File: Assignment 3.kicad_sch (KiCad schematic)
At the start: 1 part

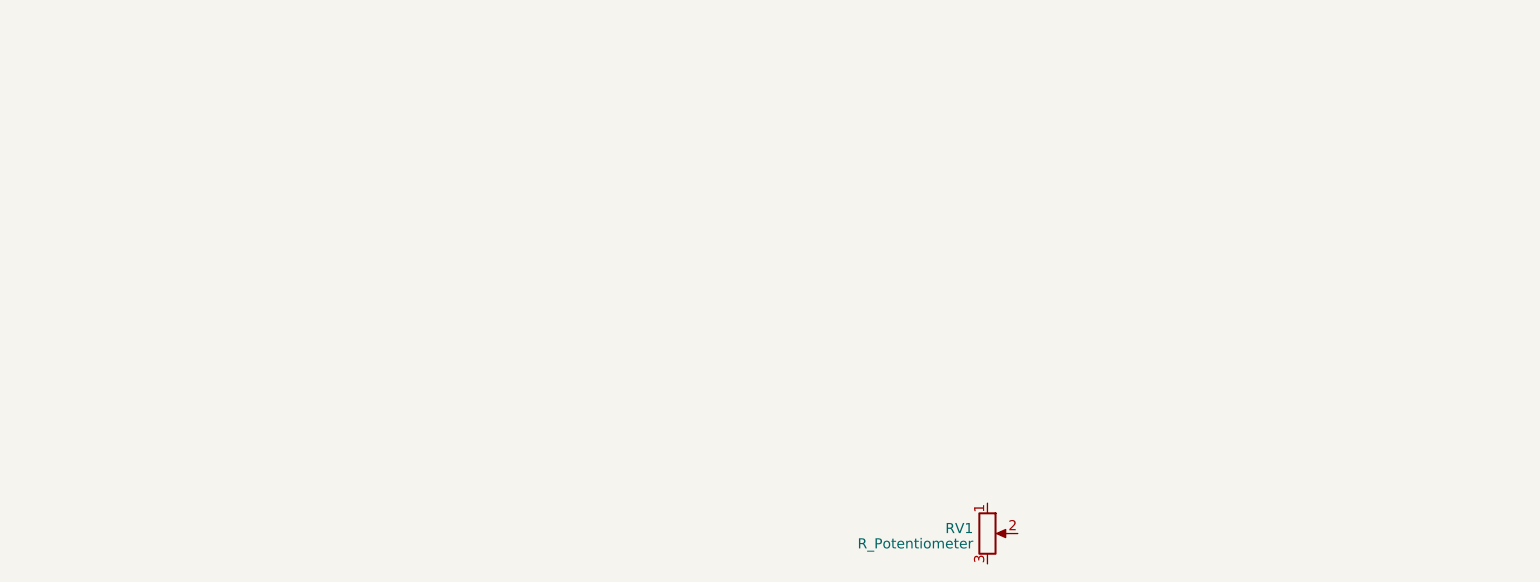
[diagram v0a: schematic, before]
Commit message: Hierarchical Sheets
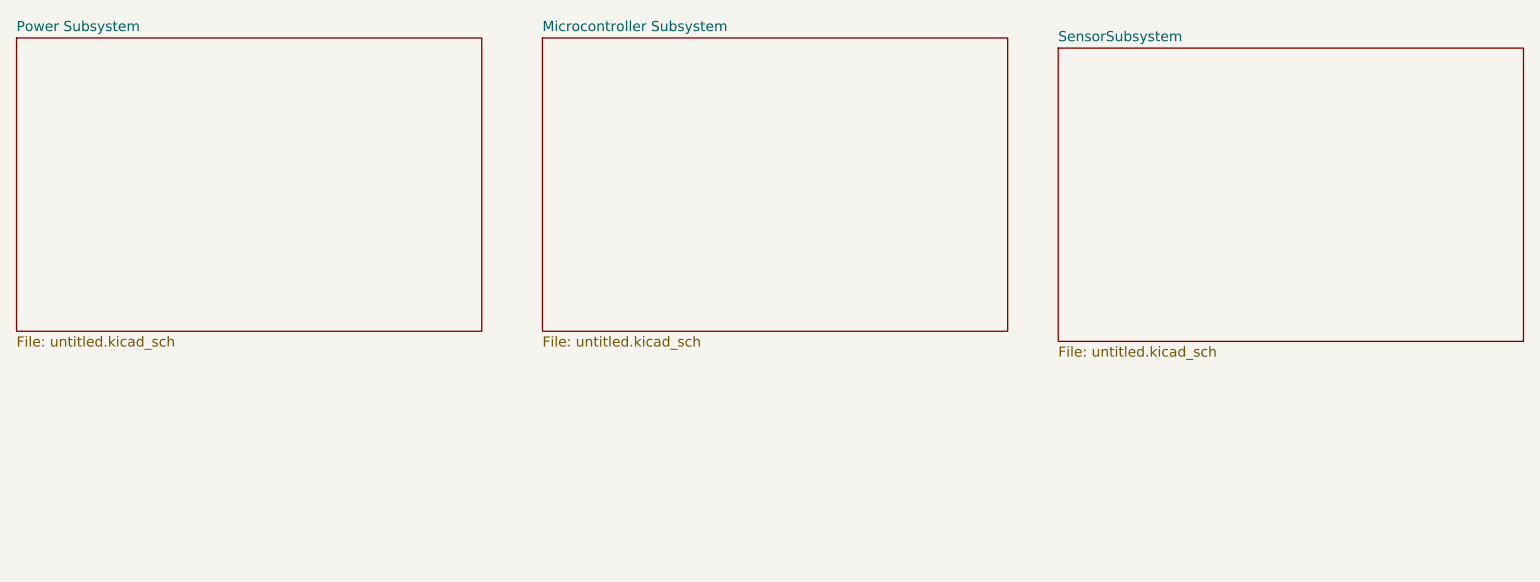
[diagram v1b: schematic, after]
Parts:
- removed RV1: R_Potentiometer, symbol Device:R_Potentiometer
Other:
- added sheet Microcontroller Subsystem (untitled.kicad_sch)
- added sheet Power Subsystem  (untitled.kicad_sch)
- added sheet SensorSubsystem (untitled.kicad_sch)
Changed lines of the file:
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@@
 (kicad_sch (version 20230121) (generator eeschema)
   (paper "A4")
-  (symbol (lib_id "Device:R_Potentiometer") (at 152.4 95.25 0) (unit 1)
-    (in_bom yes) (on_board yes) (dnp no) (fields_autoplaced)
-    (property "Reference" "RV1" (at 150.622 94.6063 0)
-      (effects (font (size 1.27 1.27)) (justify right))
+  (sheet (at 96.52 33.02) (size 58.42 36.83) (fields_autoplaced)
+    (stroke (width 0.1524) (type solid))
+    (fill (color 0 0 0 0.0000))
+    (property "Sheetname" "Microcontroller Subsystem" (at 96.52 32.3084 0)
+      (effects (font (size 1.27 1.27)) (justify left bottom))
     )
-    (property "Value" "R_Potentiometer" (at 150.622 96.5273 0)
-      (effects (font (size 1.27 1.27)) (justify right))
+    (property "Sheetfile" "untitled.kicad_sch" (at 96.52 70.4346 0)
+      (effects (font (size 1.27 1.27)) (justify left top))
     )
-    (property "Footprint" "" (at 152.4 95.25 0)
-      (effects (font (size 1.27 1.27)) hide)
-    )
-    (property "Datasheet" "~" (at 152.4 95.25 0)
-      (effects (font (size 1.27 1.27)) hide)
-    )
-    (pin "1")
-    (pin "2")
-    (pin "3")
     (instances
       (project "Assignment 3"
-        (path "/3a34ae49-7c4e-4d09-9f19-4770c7be9d9e"
-          (reference "RV1") (unit 1)
-        )
+        (path "/3a34ae49-7c4e-4d09-9f19-4770c7be9d9e" (page "3"))
       )
     )
+  )
+  (sheet (at 161.29 34.29) (size 58.42 36.83) (fields_autoplaced)
+    (stroke (width 0.1524) (type solid))
+    (fill (color 0 0 0 0.0000))
+    (property "Sheetname" "SensorSubsystem" (at 161.29 33.5784 0)
+      (effects (font (size 1.27 1.27)) (justify left bottom))
+    )
+    (property "Sheetfile" "untitled.kicad_sch" (at 161.29 71.7046 0)
+      (effects (font (size 1.27 1.27)) (justify left top))
+    )
+    (instances
+      (project "Assignment 3"
+        (path "/3a34ae49-7c4e-4d09-9f19-4770c7be9d9e" (page "4"))
+      )
+    )
+  )
+  (sheet (at 30.48 33.02) (size 58.42 36.83) (fields_autoplaced)
+    (stroke (width 0.1524) (type solid))
+    (fill (color 0 0 0 0.0000))
+    (property "Sheetname" "Power Subsystem " (at 30.48 32.3084 0)
+      (effects (font (size 1.27 1.27)) (justify left bottom))
+    )
+    (property "Sheetfile" "untitled.kicad_sch" (at 30.48 70.4346 0)
+      (effects (font (size 1.27 1.27)) (justify left top))
+    )
+    (instances
+      (project "Assignment 3"
+        (path "/3a34ae49-7c4e-4d09-9f19-4770c7be9d9e" (page "2"))
+      )
+    )

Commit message: Commit 1
This is a commit of progress that has been made
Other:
- sheet Microcontroller Subsystem renamed Bulisani
- removed sheet Power Subsystem 
- removed sheet SensorSubsystem
- added sheet Gathuku (Power Subsystem.kicad_sch)
- added sheet Zinzile (Sensor Subsystem.kicad_sch)
- sheet Bulisani: file untitled.kicad_sch -> Microcontroller Subsystem.kicad_sch
- sheet Bulisani ports: added 3V3, 5V, PA5, PA6, PA7, PF1, PF6, PF7; removed none
- company: (none) -> University of Cape Town 
- title: (none) -> EEE3088F Microcontroller Board 
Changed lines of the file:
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@@
 (kicad_sch (version 20230121) (generator eeschema)
   (paper "A4")
-  (sheet (at 96.52 33.02) (size 58.42 36.83) (fields_autoplaced)
+  (title_block
+    (title "EEE3088F Microcontroller Board ")
+    (date "2023-03-18")
+    (rev "V1")
+    (company "University of Cape Town ")
+    (comment 1 "MBZZIN003: Zinzile Mabizela ")
+    (comment 2 "MTHGAT001: Gathuku Matheri")
+    (comment 3 "NGWBUL004: Bulisani Ngwenya ")
+    (comment 4 "Group 11")
+  )
+  (junction (at 124.46 125.73) (diameter 0) (color 0 0 0 0)
+  )
+  (wire (pts (xy 187.96 151.13) (xy 209.55 151.13))
+    (stroke (width 0) (type default))
+  )
+  (wire (pts (xy 273.05 134.62) (xy 267.97 134.62))
+    (stroke (width 0) (type default))
+  )
+  (wire (pts (xy 273.05 161.29) (xy 273.05 134.62))
+    (stroke (width 0) (type default))
+  )
+  (wire (pts (xy 119.38 125.73) (xy 124.46 125.73))
+    (stroke (width 0) (type default))
+  )
+  (wire (pts (xy 124.46 125.73) (xy 124.46 106.68))
+    (stroke (width 0) (type default))
+  )
+  (wire (pts (xy 124.46 161.29) (xy 273.05 161.29))
+    (stroke (width 0) (type default))
+  )
+  (wire (pts (xy 119.38 142.24) (xy 124.46 142.24))
+    (stroke (width 0) (type default))
+  )
+  (wire (pts (xy 187.96 130.81) (xy 209.55 130.81))
+    (stroke (width 0) (type default))
+  )
+  (wire (pts (xy 273.05 106.68) (xy 273.05 125.73))
+    (stroke (width 0) (type default))
+  )
+  (wire (pts (xy 187.96 123.19) (xy 209.55 123.19))
+    (stroke (width 0) (type default))
+  )
+  (wire (pts (xy 187.96 143.51) (xy 209.55 143.51))
+    (stroke (width 0) (type default))
+  )
+  (wire (pts (xy 124.46 142.24) (xy 124.46 161.29))
+    (stroke (width 0) (type default))
+  )
+  (wire (pts (xy 187.96 147.32) (xy 209.55 147.32))
+    (stroke (width 0) (type default))
+  )
+  (wire (pts (xy 124.46 125.73) (xy 129.54 125.73))
+    (stroke (width 0) (type default))
+  )
+  (wire (pts (xy 119.38 134.62) (xy 129.54 134.62))
+    (stroke (width 0) (type default))
+  )
+  (wire (pts (xy 124.46 106.68) (xy 273.05 106.68))
+    (stroke (width 0) (type default))
+  )
+  (wire (pts (xy 273.05 125.73) (xy 267.97 125.73))
+    (stroke (width 0) (type default))
+  )
+  (wire (pts (xy 187.96 134.62) (xy 209.55 134.62))
+    (stroke (width 0) (type default))
+  )
+  (sheet (at 129.54 116.84) (size 58.42 36.83) (fields_autoplaced)
     (stroke (width 0.1524) (type solid))
     (fill (color 0 0 0 0.0000))
-    (property "Sheetname" "Microcontroller Subsystem" (at 96.52 32.3084 0)
+    (property "Sheetname" "Bulisani" (at 129.54 116.1284 0)
       (effects (font (size 1.27 1.27)) (justify left bottom))
     )
-    (property "Sheetfile" "untitled.kicad_sch" (at 96.52 70.4346 0)
+    (property "Sheetfile" "Microcontroller Subsystem.kicad_sch" (at 129.54 154.2546 0)
       (effects (font (size 1.27 1.27)) (justify left top))
+    )
+    (pin "5V" input (at 129.54 134.62 180)
+      (effects (font (size 1.27 1.27)) (justify left))
+    )
+    (pin "PA5" input (at 187.96 123.19 0)
+      (effects (font (size 1.27 1.27)) (justify right))
+    )
+    (pin "PA6" output (at 187.96 130.81 0)
+      (effects (font (size 1.27 1.27)) (justify right))
+    )
+    (pin "3V3" input (at 129.54 125.73 180)
+      (effects (font (size 1.27 1.27)) (justify left))
+    )
+    (pin "PF7" input (at 187.96 151.13 0)
+      (effects (font (size 1.27 1.27)) (justify right))
+    )
+    (pin "PF6" input (at 187.96 147.32 0)
+      (effects (font (size 1.27 1.27)) (justify right))
+    )
+    (pin "PF1" input (at 187.96 143.51 0)
+      (effects (font (size 1.27 1.27)) (justify right))
+    )
+    (pin "PA7" output (at 187.96 134.62 0)
+      (effects (font (size 1.27 1.27)) (justify right))
     )
     (instances
@@
     )
   )
-  (sheet (at 161.29 34.29) (size 58.42 36.83) (fields_autoplaced)
+  (sheet (at 209.55 116.84) (size 58.42 36.83) (fields_autoplaced)
     (stroke (width 0.1524) (type solid))
     (fill (color 0 0 0 0.0000))
-    (property "Sheetname" "SensorSubsystem" (at 161.29 33.5784 0)
+    (property "Sheetname" "Zinzile" (at 209.55 116.1284 0)
       (effects (font (size 1.27 1.27)) (justify left bottom))
     )
-    (property "Sheetfile" "untitled.kicad_sch" (at 161.29 71.7046 0)
+    (property "Sheetfile" "Sensor Subsystem.kicad_sch" (at 209.55 154.2546 0)
       (effects (font (size 1.27 1.27)) (justify left top))
+    )
+    (pin "PA7" input (at 209.55 134.62 180)
+      (effects (font (size 1.27 1.27)) (justify left))
+    )
+    (pin "3V3" input (at 267.97 125.73 0)
+      (effects (font (size 1.27 1.27)) (justify right))
+    )
+    (pin "PF6" input (at 209.55 130.81 180)
+      (effects (font (size 1.27 1.27)) (justify left))
+    )
+    (pin "PF1" output (at 209.55 143.51 180)
+      (effects (font (size 1.27 1.27)) (justify left))
+    )
+    (pin "PF7" output (at 209.55 151.13 180)
+      (effects (font (size 1.27 1.27)) (justify left))
+    )
+    (pin "PA6" output (at 209.55 147.32 180)
+      (effects (font (size 1.27 1.27)) (justify left))
+    )
+    (pin "V_Batt" input (at 267.97 134.62 0)
+      (effects (font (size 1.27 1.27)) (justify right))
+    )
+    (pin "PA5" output (at 209.55 123.19 180)
+      (effects (font (size 1.27 1.27)) (justify left))
     )
     (instances
@@
     )
   )
-  (sheet (at 30.48 33.02) (size 58.42 36.83) (fields_autoplaced)
+  (sheet (at 60.96 116.84) (size 58.42 36.83) (fields_autoplaced)
     (stroke (width 0.1524) (type solid))
     (fill (color 0 0 0 0.0000))
-    (property "Sheetname" "Power Subsystem " (at 30.48 32.3084 0)
+    (property "Sheetname" "Gathuku" (at 60.96 116.1284 0)
       (effects (font (size 1.27 1.27)) (justify left bottom))
     )
-    (property "Sheetfile" "untitled.kicad_sch" (at 30.48 70.4346 0)
+    (property "Sheetfile" "Power Subsystem.kicad_sch" (at 60.96 154.2546 0)
       (effects (font (size 1.27 1.27)) (justify left top))
     )
+    (pin "VBatt" output (at 119.38 142.24 0)
+      (effects (font (size 1.27 1.27)) (justify right))
+    )
+    (pin "5V" output (at 119.38 134.62 0)
+      (effects (font (size 1.27 1.27)) (justify right))
+    )
+    (pin "3V3" input (at 119.38 125.73 0)
+      (effects (font (size 1.27 1.27)) (justify right))
+    )
     (instances
